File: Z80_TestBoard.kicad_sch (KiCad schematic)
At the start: 23 parts, among them J1 ICSP, J2 UART, J3 I2C, J5 CLK_SW, J6 M1_O, J7 USB_B_Mini, U1 Z84C00_PLCC, U2 PIC18F4520-xP, Y2 Crystal, Y3 CXO_DIP8

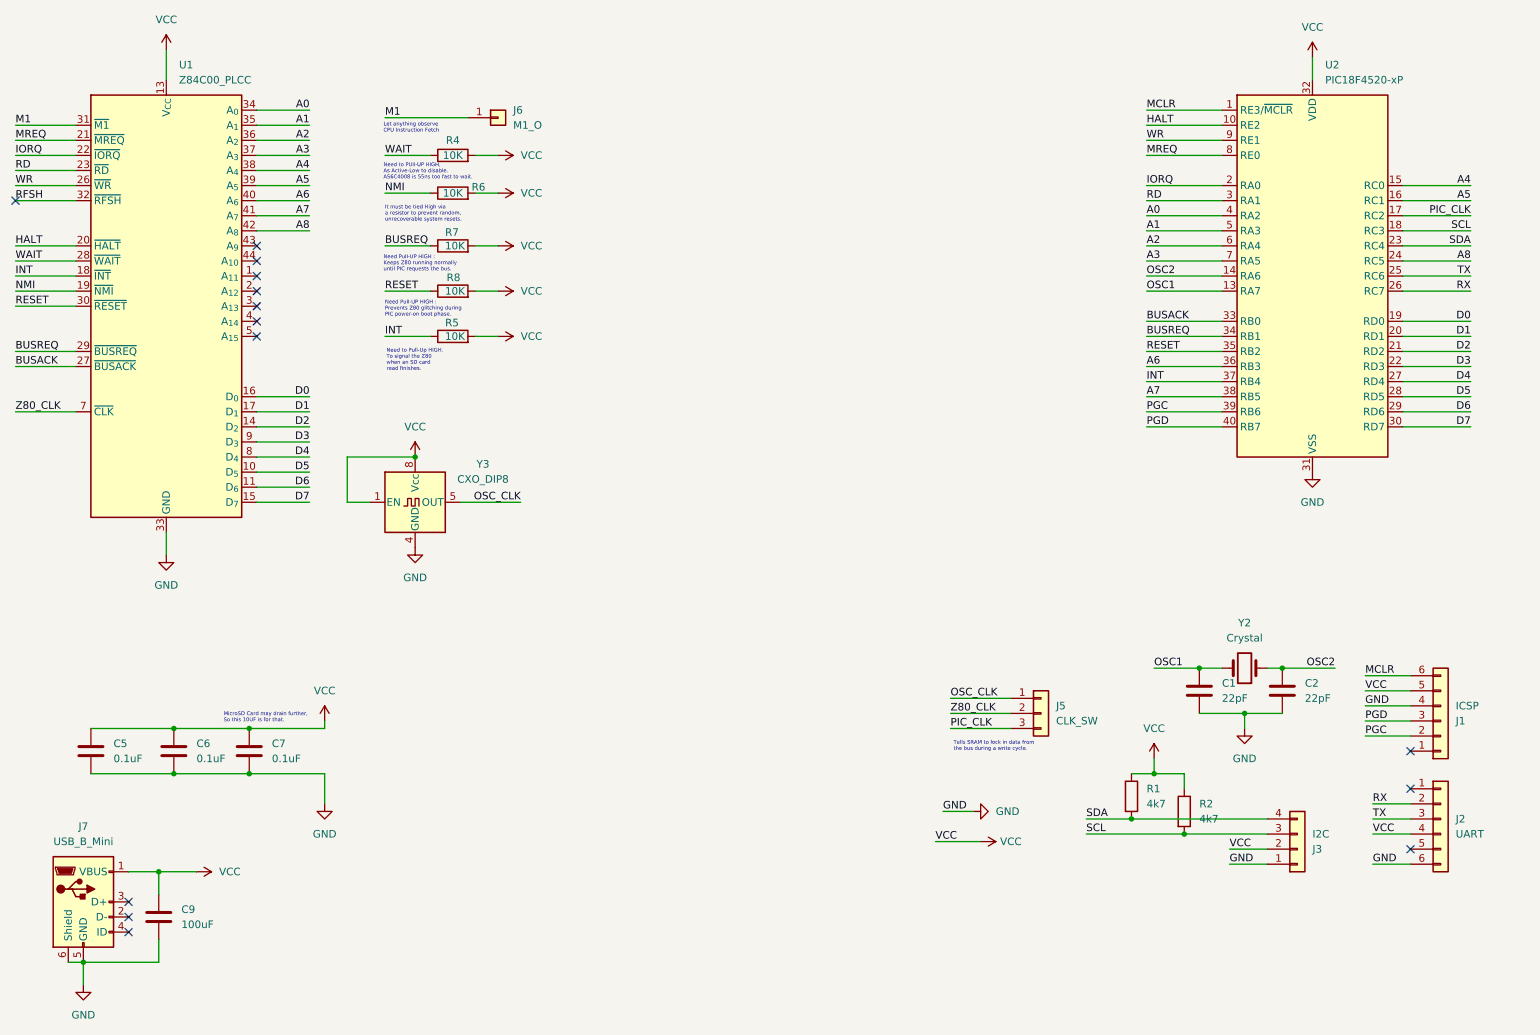
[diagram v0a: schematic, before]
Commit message: Refine with NE555P + LED.
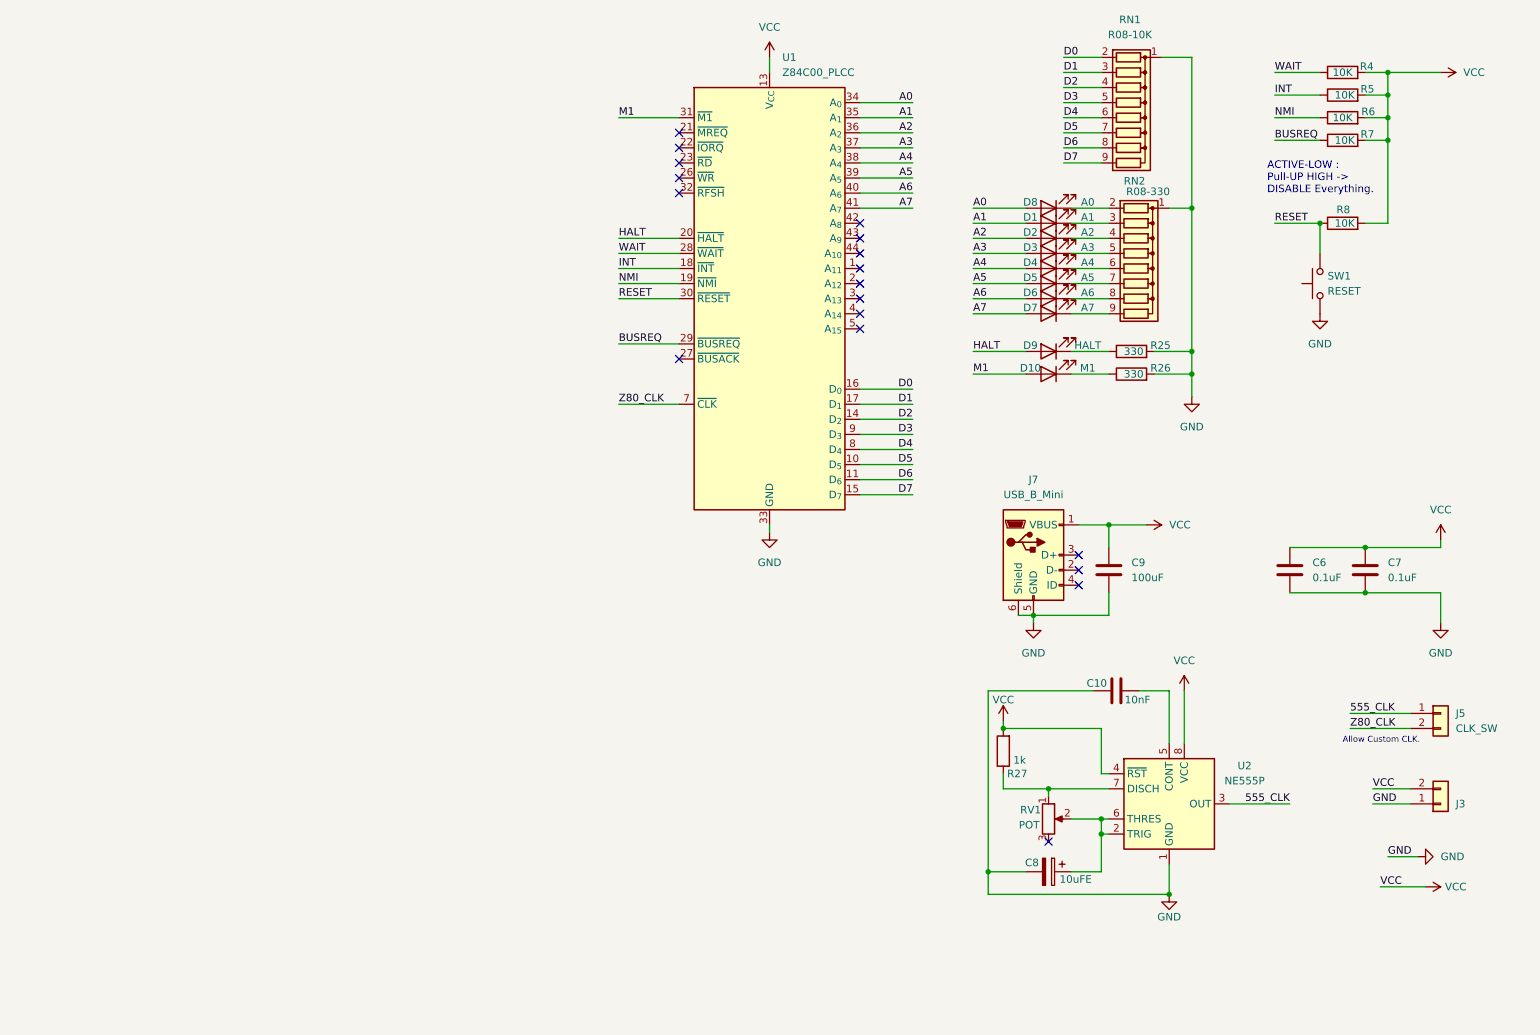
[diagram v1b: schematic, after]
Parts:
- removed C1, C2: 22pF, Capacitor_THT:C_Disc_D3.4mm_W2.1mm_P2.50mm, symbol Device:C
- removed C5: 0.1uF, Capacitor_THT:C_Disc_D3.4mm_W2.1mm_P2.50mm, symbol Device:C
- removed J1: ICSP, Connector_PinHeader_2.54mm:PinHeader_1x06_P2.54mm_Horizontal, symbol Connector_Generic:Conn_01x06
- removed J2: UART, Connector_PinHeader_2.54mm:PinHeader_1x06_P2.54mm_Vertical, symbol Connector_Generic:Conn_01x06
- removed J6: M1_O, Connector_PinHeader_2.54mm:PinHeader_1x01_P2.54mm_Vertical, symbol Connector_Generic:Conn_01x01
- removed R1, R2: 4k7, Resistor_THT:R_Axial_DIN0207_L6.3mm_D2.5mm_P10.16mm_Horizontal, symbol Device:R
- removed U2: PIC18F4520-xP, Package_DIP:DIP-40_W15.24mm, symbol MCU_Microchip_PIC18:PIC18F4520-xP
- removed Y2: Crystal, Crystal:Crystal_HC49-4H_Vertical, symbol Device:Crystal
- removed Y3: CXO_DIP8, Oscillator:Oscillator_DIP-8, symbol Oscillator:CXO_DIP8
- added C10: 10nF, Capacitor_THT:C_Disc_D3.4mm_W2.1mm_P2.50mm, symbol Device:C
- added C8: 10uFE, Capacitor_THT:C_Radial_D4.0mm_H5.0mm_P1.50mm, symbol Device:C_Polarized
- added D1: A1, LED_THT:LED_D3.0mm, symbol Device:LED
- added D10: M1, LED_THT:LED_D3.0mm, symbol Device:LED
- added D2: A2, LED_THT:LED_D3.0mm, symbol Device:LED
- added D3: A3, LED_THT:LED_D3.0mm, symbol Device:LED
- added D4: A4, LED_THT:LED_D3.0mm, symbol Device:LED
- added D5: A5, LED_THT:LED_D3.0mm, symbol Device:LED
- added D6: A6, LED_THT:LED_D3.0mm, symbol Device:LED
- added D7: A7, LED_THT:LED_D3.0mm, symbol Device:LED
- added D8: A0, LED_THT:LED_D3.0mm, symbol Device:LED
- added D9: HALT, LED_THT:LED_D3.0mm, symbol Device:LED
- added R25, R26: 330, Resistor_THT:R_Axial_DIN0207_L6.3mm_D2.5mm_P10.16mm_Horizontal, symbol Device:R
- added R27: 1k, Resistor_THT:R_Axial_DIN0207_L6.3mm_D2.5mm_P10.16mm_Horizontal, symbol Device:R
- added RN1: R08-10K, Resistor_THT:R_Array_SIP9, symbol Device:R_Network08
- added RN2: R08-330, Resistor_THT:R_Array_SIP9, symbol Device:R_Network08
- added RV1: POT, Potentiometer_THT:Potentiometer_Bourns_PTV09A-1_Single_Vertical, symbol Device:R_Potentiometer
- added SW1: RESET, Button_Switch_THT:SW_PUSH_6mm, symbol Switch:SW_Push
- added U2: NE555P, Package_DIP:DIP-8_W7.62mm, symbol Timer:NE555P
- J3: value I2C -> PWR; footprint Connector_PinHeader_2.54mm:PinHeader_1x04_P2.54mm_Vertical -> Connector_PinHeader_2.54mm:PinHeader_1x02_P2.54mm_Vertical; symbol Connector_Generic:Conn_01x04 -> Connector_Generic:Conn_01x02
- J5: footprint Connector_PinHeader_2.54mm:PinHeader_1x03_P2.54mm_Vertical -> Connector_PinHeader_2.54mm:PinHeader_1x02_P2.54mm_Vertical; symbol Connector_Generic:Conn_01x03 -> Connector_Generic:Conn_01x02
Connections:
- net A0: now also D8.2 (A)
- net A1: now also D1.2 (A)
- net A2: now also D2.2 (A)
- net A3: now also D3.2 (A)
- net A4: now also D4.2 (A)
- net A5: now also D5.2 (A)
- net A6: now also D6.2 (A)
- net A7: now also D7.2 (A)
- net D0: now also RN1.2 (R1)
- net D1: now also RN1.3 (R2)
- net D2: now also RN1.4 (R3)
- net D3: now also RN1.5 (R4)
- net D4: now also RN1.6 (R5)
- net D5: now also RN1.7 (R6)
- net D6: now also RN1.8 (R7)
- net D7: now also RN1.9 (R8)
- net GND: now also C10.2, C8.2, R25.2, R26.2, RN1.1 (common), RN2.1 (common), SW1.1, U2.1 (GND)
- net HALT: now also D9.2 (A)
- net M1: now also D10.2 (A)
- net RESET: now also SW1.2
- net VCC: now also R27.2, U2.4 (~{RST}), U2.8 (VCC)
- net A8: no longer names the net of U1.42 (A_{8})
- net BUSACK: no longer names the net of U1.27 (~{BUSACK})
- net IORQ: no longer names the net of U1.22 (~{IORQ})
- net MREQ: no longer names the net of U1.21 (~{MREQ})
- net OSC_CLK renamed 555_CLK
- net 555_CLK: now also U2.3 (OUT)
- removed net PIC_CLK: J5.3 (Pin_3)
- net RD: no longer names the net of U1.23 (~{RD})
- net RFSH: no longer names the net of U1.32 (~{RFSH})
- removed net SCL: J3.3 (Pin_3)
- removed net SDA: J3.4 (Pin_4)
- net WR: no longer names the net of U1.26 (~{WR})
- new net: D8.1 (K), RN2.2 (R1)
- new net: C8.1, RV1.2, U2.2 (TRIG), U2.6 (THRES)
- new net: C10.1, U2.5 (CONT)
- new net: R27.1, RV1.1, U2.7 (DISCH)
- new net: D2.1 (K), RN2.4 (R3)
- new net: D4.1 (K), RN2.6 (R5)
- new net: D9.1 (K), R25.1
- new net: D6.1 (K), RN2.8 (R7)
- new net: D3.1 (K), RN2.5 (R4)
- new net: D10.1 (K), R26.1
- new net: D1.1 (K), RN2.3 (R2)
- new net: D5.1 (K), RN2.7 (R6)
- new net: D7.1 (K), RN2.9 (R8)
- no-connect marks 14 -> 18
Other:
- note added: "ACTIVE-LOW : Pull-UP HIGH -> DISABLE Everything."
- note added: "Allow Custom CLK."
- note removed: "It must be tied High via a resistor to prevent random, unrecoverable system resets."
- note removed: "Let anything observe CPU Instruction Fetch"
- note removed: "MicroSD Card may drain further, So this 10UF is for that."
- note removed: "Need Pull-UP HIGH : Keeps Z80 running normally until PIC requests the bus."
- note removed: "Need Pull-UP HIGH : Prevents Z80 glitching during PIC power-on boot phase."
- note removed: "Need to PUll-UP HIGH, As Active-Low to disable. AS6C4008 is 55ns too fast to wait."
- note removed: "Need to Pull-Up HIGH. To signal the Z80 when an SD card read finishes."
- note removed: "Tells SRAM to lock in data from the bus during a write cycle."
- moved on the sheet: C6, C7, C9, J7, R4, R5, R6, R7, R8, U1

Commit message: finish routing/layout.
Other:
- title: Z80-PLCC TestBoard -> Z80-PLCC-NOP-TEST
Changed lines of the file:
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@@
 	(paper "A4")
 	(title_block
-		(title "Z80-PLCC TestBoard")
+		(title "Z80-PLCC-NOP-TEST")
 	)
 	(text "ACTIVE-LOW :\nPull-UP HIGH -> \nDISABLE Everything."

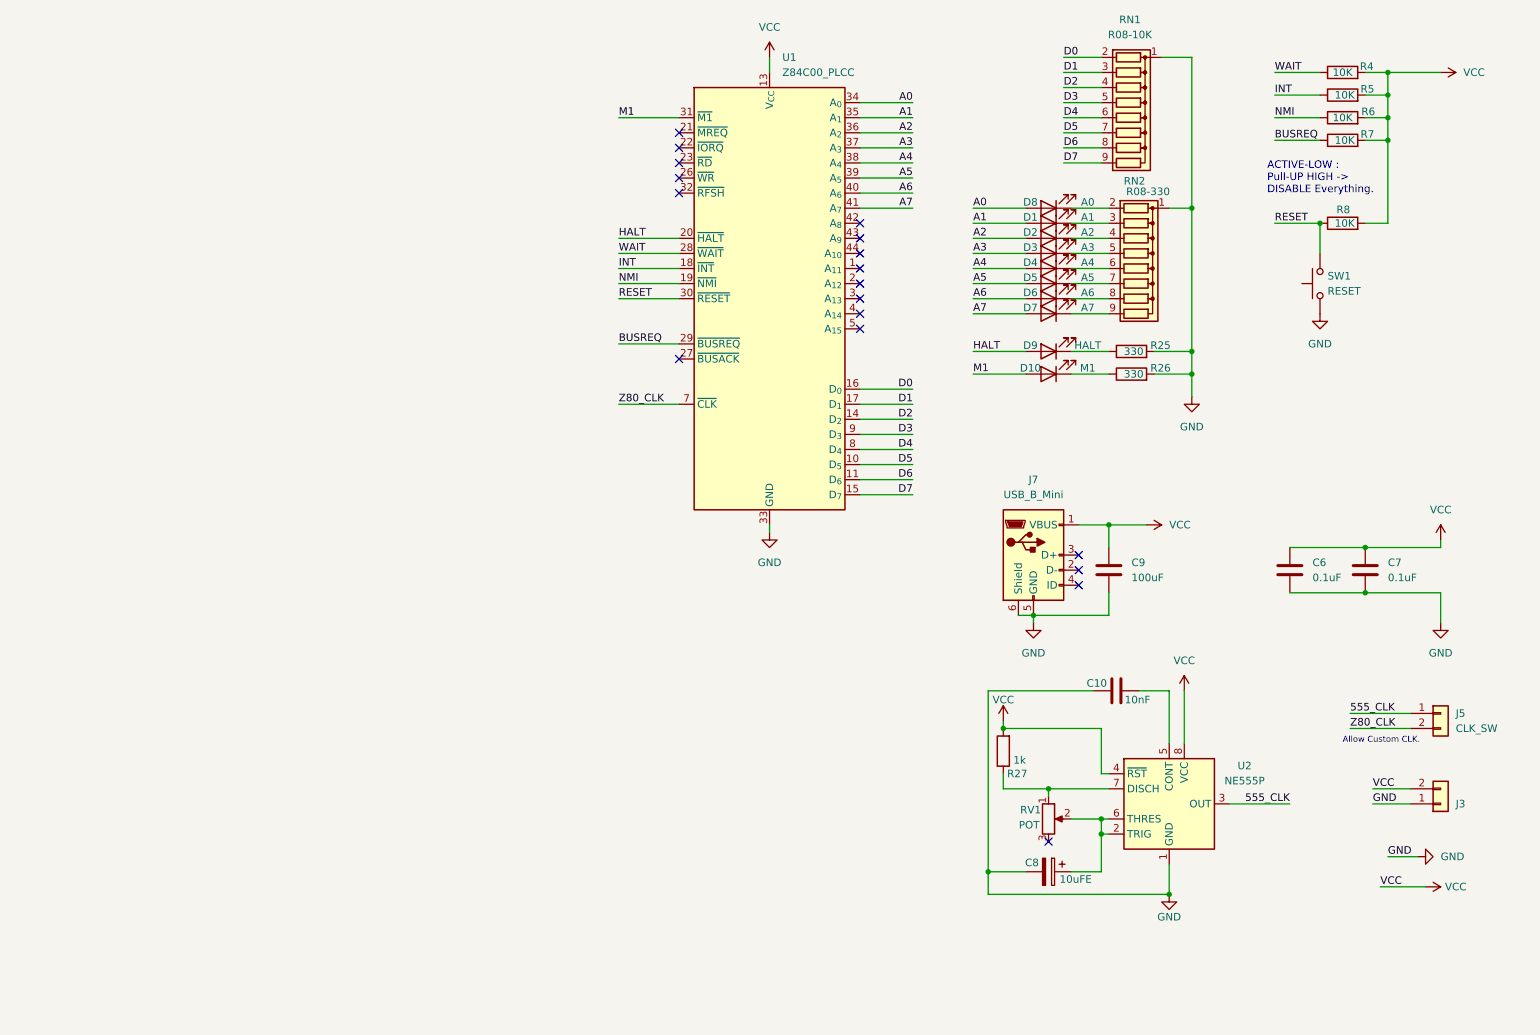
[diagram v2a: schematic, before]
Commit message: add SOP28-DIP28 + LED-Board.
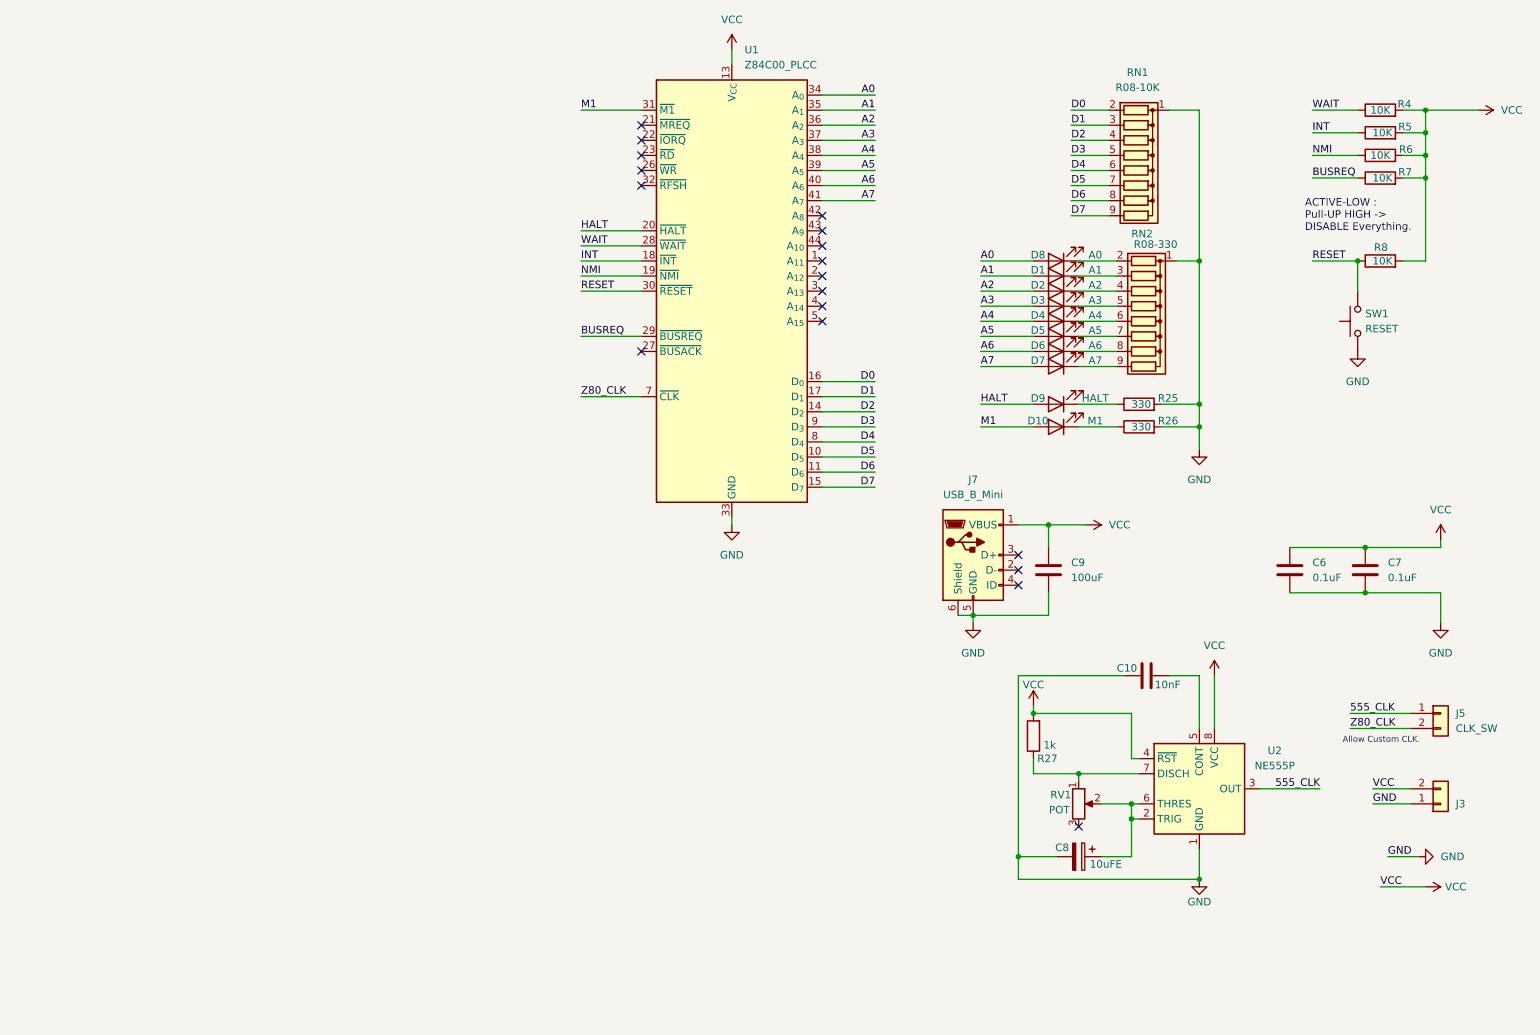
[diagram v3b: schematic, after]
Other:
- moved on the sheet: C10, C8, C9, D1, D10, D2, D3, D4, D5, D6, D7, D8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
